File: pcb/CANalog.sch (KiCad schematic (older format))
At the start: 81 parts, among them J1 PWR, J4 STM_PROG, J5 ESP_PROG, J6 AOUT, J7 CAN, Q1 DMP3099L-7, SW1 RESET, SW2 ESP_PROG, U1 BL9342, U2 MIC5504-3.3YM5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

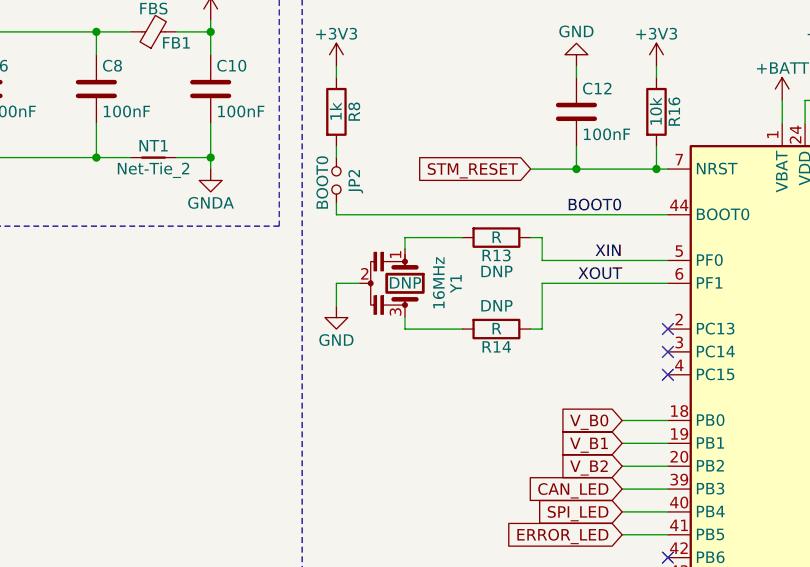
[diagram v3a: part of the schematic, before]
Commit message: update iBom with DNP fields missing
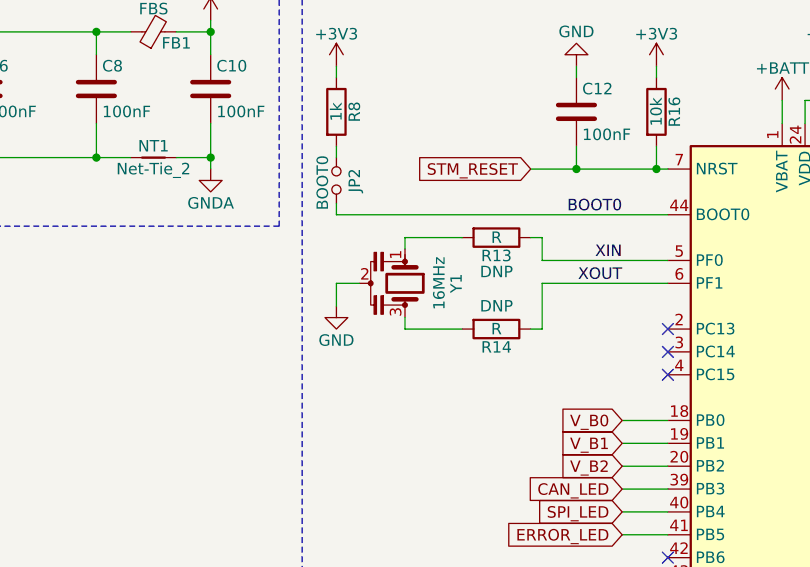
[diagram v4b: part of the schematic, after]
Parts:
- Y1: Population DNP -> (none)
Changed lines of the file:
@@
 F 2 "Crystal:Resonator_SMD_muRata_CSTxExxV-3Pin_3.0x1.1mm" H 6625 6200 50  0001 C CNN
 F 3 "https://www.mouser.com/datasheet/2/281/murata_04192018_CSTN_CeramResonCERAL-1323383.pdf" H 6625 6200 50  0001 C CNN
-F 4 "DNP" V 6650 6200 50  0000 C CNN "Population"
-F 5 "CSTNE16M0VH3C000R0 " H 6650 6200 50  0001 C CNN "MPN"
-F 6 "Murata Electronics" H 6650 6200 50  0001 C CNN "Manufacture"
-F 7 "81-CSTNE16M0VH3C000R " H 6650 6200 50  0001 C CNN "SPN"
-F 8 "Mouser" H 6650 6200 50  0001 C CNN "Supplier"
-F 9 "https://www.mouser.com/ProductDetail/81-CSTNE16M0VH3C000R" H 6650 6200 50  0001 C CNN "Supplier Link"
+F 4 "CSTNE16M0VH3C000R0 " H 6650 6200 50  0001 C CNN "MPN"
+F 5 "Murata Electronics" H 6650 6200 50  0001 C CNN "Manufacture"
+F 6 "81-CSTNE16M0VH3C000R " H 6650 6200 50  0001 C CNN "SPN"
+F 7 "Mouser" H 6650 6200 50  0001 C CNN "Supplier"
+F 8 "https://www.mouser.com/ProductDetail/81-CSTNE16M0VH3C000R" H 6650 6200 50  0001 C CNN "Supplier Link"
 	1    6650 6200
 	0    1    1    0

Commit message: fix ibom missing R21
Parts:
- R21: Population DNP -> (none)
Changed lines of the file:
@@
 F 2 "Resistor_SMD:R_0603_1608Metric" V 11580 2000 50  0001 C CNN
 F 3 "~" H 11650 2000 50  0001 C CNN
-F 4 "DNP" H 11650 2000 50  0001 C CNN "Population"
 	1    11650 2000
 	0    1    1    0

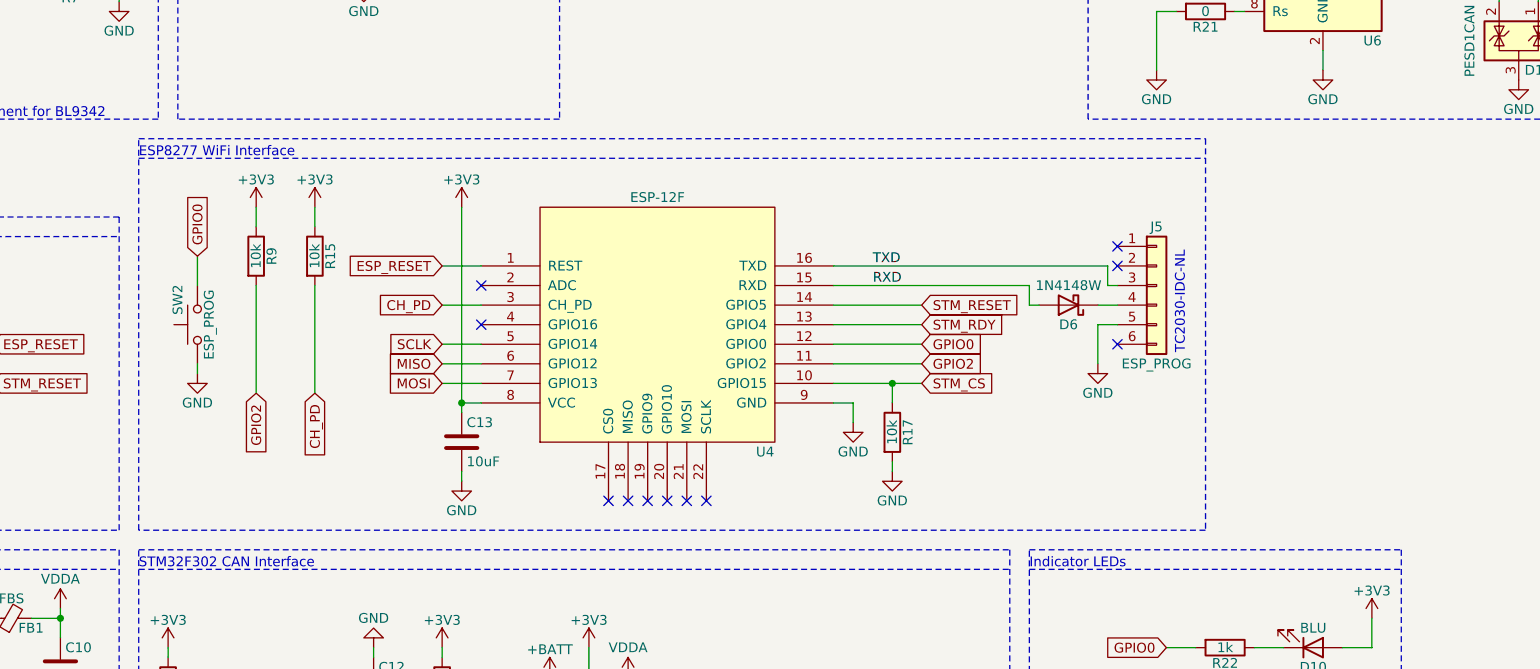
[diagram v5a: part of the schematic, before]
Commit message: added resistor between STM32 reset land ESP8266 GPIO15
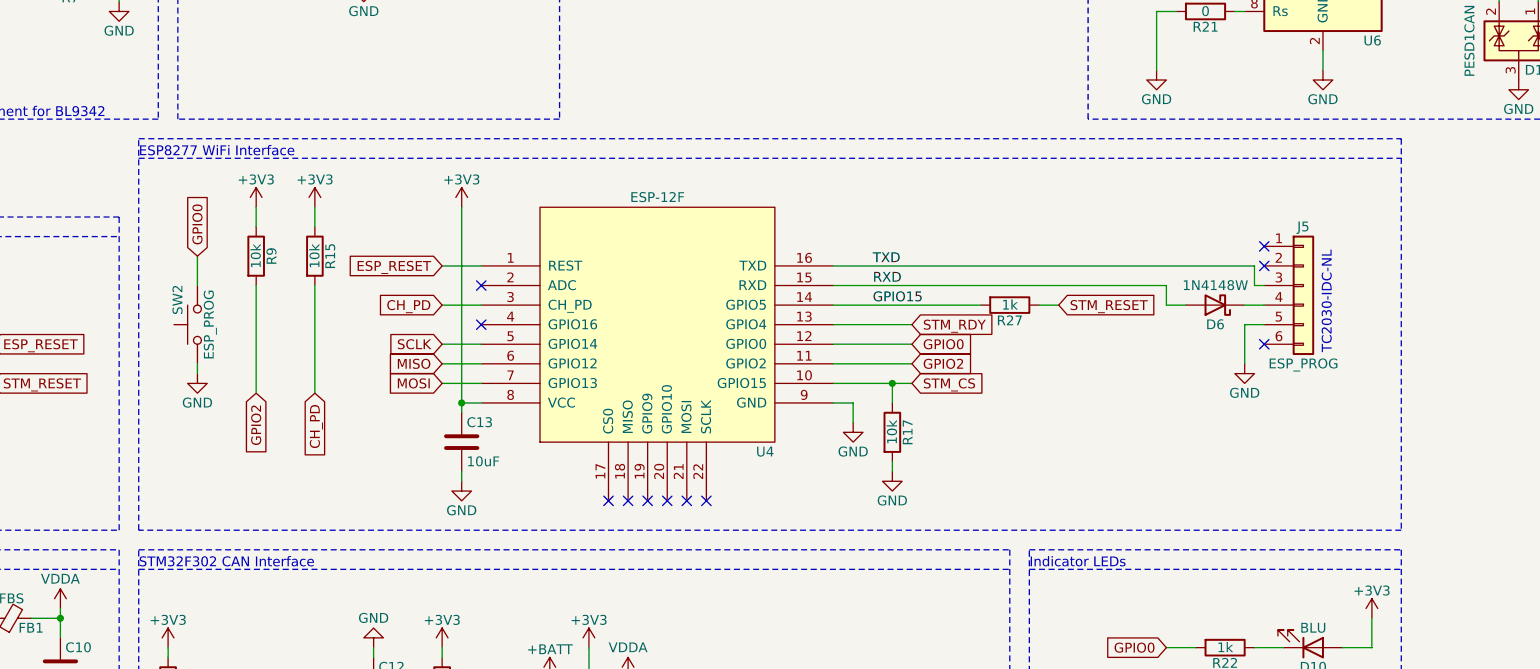
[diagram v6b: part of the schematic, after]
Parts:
- added R27: 1k, Resistor_SMD:R_0603_1608Metric, symbol Device:R
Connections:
- net STM_RESET: now also R27.1; no longer U4.14 (GPIO5)
- new net GPIO15: R27.2, U4.14 (GPIO5)
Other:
- moved on the sheet: D6, J5
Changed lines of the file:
@@
 $EndComp
 Wire Notes Line
-	11650 2650 11650 4650
+	12650 2650 12650 4650
 Text Label 9950 3400 0    50   ~ 0
 RXD
 Wire Wire Line
-	10750 3500 10750 3400
+	11450 3500 11450 3400
 Text Label 9950 3300 0    50   ~ 0
 TXD
 Wire Wire Line
-	9750 3300 11150 3300
+	9750 3300 11900 3300
 Wire Wire Line
 	10050 4350 10050 4300
@@
 Wire Wire Line
 	6800 3400 6800 3950
-Text GLabel 10200 3800 2    50   Input ~ 0
+Text GLabel 10150 3800 2    50   Input ~ 0
 GPIO2
 Wire Wire Line
-	10200 3800 9750 3800
+	10150 3800 9750 3800
 Text GLabel 6800 3950 3    50   Input ~ 0
 GPIO2
@@
 NoConn ~ 9000 4500
 NoConn ~ 9100 4500
-Text GLabel 10200 3900 2    50   Input ~ 0
+Text GLabel 10150 3900 2    50   Input ~ 0
 STM_CS
 Wire Wire Line
-	10200 3900 10050 3900
+	10150 3900 10050 3900
 $Comp
 L Switch:SW_Push SW2
@@
 ESP_RESET
 Wire Wire Line
-	9750 3700 10200 3700
-Text GLabel 10200 3700 2    50   Input ~ 0
+	9750 3700 10150 3700
+Text GLabel 10150 3700 2    50   Input ~ 0
 GPIO0
 $Comp
@@
 MOSI
 NoConn ~ 7950 3600
-Wire Wire Line
-	9750 3400 10750 3400
-Text GLabel 10200 3600 2    50   Input ~ 0
+Text GLabel 10150 3600 2    50   Input ~ 0
 STM_RDY
 Wire Wire Line
-	10200 3600 9750 3600
-Wire Wire Line
-	9750 3500 10200 3500
-Wire Notes Line
-	6200 2750 11650 2750
-Wire Notes Line
-	11650 4650 6200 4650
+	10150 3600 9750 3600
+Wire Notes Line
+	6200 2750 12650 2750
+Wire Notes Line
+	12650 4650 6200 4650
 Wire Notes Line
 	6200 4650 6200 2650
 Wire Notes Line
-	6200 2650 11650 2650
+	6200 2650 12650 2650
 $Comp
 L Connector_Generic:Conn_01x06 J5
 U 1 1 60FEC2BA
-P 11400 3400
-F 0 "J5" H 11400 3700 50  0000 C CNN
-F 1 "ESP_PROG" H 11400 3000 50  0000 C CNN
-F 2 "Connector:Tag-Connect_TC2030-IDC-NL_2x03_P1.27mm_Vertical" H 11400 3400 50  0001 C CNN
-F 3 "~" H 11400 3400 50  0001 C CNN
-F 4 "DNP" H 11400 3400 50  0001 C CNN "Population"
-	1    11400 3400
+P 12150 3400
+F 0 "J5" H 12150 3700 50  0000 C CNN
+F 1 "ESP_PROG" H 12150 3000 50  0000 C CNN
+F 2 "Connector:Tag-Connect_TC2030-IDC-NL_2x03_P1.27mm_Vertical" H 12150 3400 50  0001 C CNN
+F 3 "~" H 12150 3400 50  0001 C CNN
+F 4 "DNP" H 12150 3400 50  0001 C CNN "Population"
+	1    12150 3400
 	1    0    0    -1
 $EndComp
@@
 L power:GND #PWR049
 U 1 1 61023622
-P 11100 3800
-F 0 "#PWR049" H 11100 3550 50  0001 C CNN
-F 1 "GND" H 11100 3650 50  0000 C CNN
-F 2 "" H 11100 3800 50  0001 C CNN
-F 3 "" H 11100 3800 50  0001 C CNN
-	1    11100 3800
-	1    0    0    -1
-$EndComp
-NoConn ~ 11200 3200
-NoConn ~ 11200 3700
-NoConn ~ 11200 3300
-Wire Wire Line
-	10750 3500 10800 3500
-Wire Wire Line
-	11150 3400 11150 3300
+P 11850 3800
+F 0 "#PWR049" H 11850 3550 50  0001 C CNN
+F 1 "GND" H 11850 3650 50  0000 C CNN
+F 2 "" H 11850 3800 50  0001 C CNN
+F 3 "" H 11850 3800 50  0001 C CNN
+	1    11850 3800
+	1    0    0    -1
+$EndComp
+NoConn ~ 11950 3200
+NoConn ~ 11950 3700
+NoConn ~ 11950 3300
+Wire Wire Line
+	11450 3500 11550 3500
+Wire Wire Line
+	11900 3400 11900 3300
 Wire Notes Line
 	12650 6700 12650 9100
@@
 Text GLabel 5450 3900 2    50   Input ~ 0
 STM_RESET
-Text GLabel 10200 3500 2    50   Input ~ 0
+Text GLabel 10900 3500 2    50   Input ~ 0
 STM_RESET
 Wire Wire Line
@@
 L Device:D_Schottky D6
 U 1 1 606DDDEA
-P 10950 3500
-F 0 "D6" H 10950 3600 50  0000 C CNN
-F 1 "1N4148W" H 10950 3400 50  0000 C CNN
-F 2 "Diode_SMD:D_SOD-123" H 10950 3500 50  0001 C CNN
-F 3 "https://datasheet.lcsc.com/szlcsc/1809052017_MDD-Microdiode-Electronics-1N4148W_C84367.pdf" H 10950 3500 50  0001 C CNN
-F 4 "1N4148W" H 10950 3500 50  0001 C CNN "MPN"
-F 5 "Microdiode Electronics" H 10950 3500 50  0001 C CNN "Manufacture"
-F 6 "C84367" H 10950 3500 50  0001 C CNN "SPN"
-F 7 "LCSC" H 10950 3500 50  0001 C CNN "Supplier"
-F 8 "https://lcsc.com/product-detail/Switching-Diode_MDD-Microdiode-Electronics-1N4148W_C84367.html" H 10950 3500 50  0001 C CNN "Supplier Link"
-	1    10950 3500
+P 11700 3500
+F 0 "D6" H 11700 3600 50  0000 C CNN
+F 1 "1N4148W" H 11700 3400 50  0000 C CNN
+F 2 "Diode_SMD:D_SOD-123" H 11700 3500 50  0001 C CNN
+F 3 "https://datasheet.lcsc.com/szlcsc/1809052017_MDD-Microdiode-Electronics-1N4148W_C84367.pdf" H 11700 3500 50  0001 C CNN
+F 4 "1N4148W" H 11700 3500 50  0001 C CNN "MPN"
+F 5 "Microdiode Electronics" H 11700 3500 50  0001 C CNN "Manufacture"
+F 6 "C84367" H 11700 3500 50  0001 C CNN "SPN"
+F 7 "LCSC" H 11700 3500 50  0001 C CNN "Supplier"
+F 8 "https://lcsc.com/product-detail/Switching-Diode_MDD-Microdiode-Electronics-1N4148W_C84367.html" H 11700 3500 50  0001 C CNN "Supplier Link"
+	1    11700 3500
 	-1   0    0    1
 $EndComp
@@
 NoConn ~ 9100 7700
 Wire Wire Line
-	11100 3800 11100 3600
-Wire Wire Line
-	11100 3600 11200 3600
-Wire Wire Line
-	11200 3400 11150 3400
-Wire Wire Line
-	11100 3500 11200 3500
-Text Notes 11550 3750 1    50   ~ 0
+	11850 3800 11850 3600
+Wire Wire Line
+	11850 3600 11950 3600
+Wire Wire Line
+	11950 3400 11900 3400
+Wire Wire Line
+	11850 3500 11950 3500
+Text Notes 12300 3750 1    50   ~ 0
 TC2030-IDC-NL
 Text Notes 10550 8450 1    50   ~ 0
@@
 Wire Wire Line
 	9300 8300 9300 8500
+Wire Wire Line
+	9750 3500 10500 3500
+Wire Wire Line
+	10800 3500 10900 3500
+Wire Wire Line
+	9750 3400 11450 3400
+Text Label 9950 3500 0    50   ~ 0
+GPIO15
+$Comp
+L Device:R R27
+U 1 1 611F4478
+P 10650 3500
+F 0 "R27" V 10730 3500 50  0000 C CNN
+F 1 "1k" V 10650 3500 50  0000 C CNN
+F 2 "Resistor_SMD:R_0603_1608Metric" V 10580 3500 50  0001 C CNN
+F 3 "https://www.yageo.com/upload/media/product/productsearch/datasheet/rchip/PYu-RC_Group_51_RoHS_L_11.pdf" H 10650 3500 50  0001 C CNN
+F 4 "RC0603JR-071KL" H 10650 3500 50  0001 C CNN "MPN"
+F 5 "YAGEO" H 10650 3500 50  0001 C CNN "Manufacture"
+F 6 "311-1.0KGRCT-ND" H 10650 3500 50  0001 C CNN "SPN"
+F 7 "DigiKey" H 10650 3500 50  0001 C CNN "Supplier"
+F 8 "https://www.digikey.com/en/products/detail/yageo/RC0603JR-071KL/726677?s=N4IgTCBcDaIMwEYEFoEDoAMBrA5gJwGMAXZAOwBMQBdAXyA" H 10650 3500 50  0001 C CNN "Supplier Link"
+	1    10650 3500
+	0    1    1    0
+$EndComp
 $EndSCHEMATC

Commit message: add 16bit DAC
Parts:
- removed U5: OPA330xxDBV, Package_TO_SOT_SMD:SOT-23-5, symbol Amplifier_Operational:OPA330xxDBV
- added C19: 100nF, C_0603_1608Metric, symbol Device:C
- added R28: 1k, Resistor_SMD:R_0603_1608Metric, symbol Device:R
- added U5: DAC80501ZDGSR, Package_SO:VSSOP-10_3x3mm_P0.5mm, symbol pl_DAC:DAC80501ZDGSR
- R11: Population DNP -> (none)
- R12: Population (none) -> DNP
- R18: value 120k -> 10k; MPN RT0603BRD07120KL -> RC0603JR-0710KL; Population (none) -> DNP; SPN C705720 -> C99198; Supplier Link https://lcsc.com/product-detail/Chip-Resistor-Surface-Mount_YAGEO-RT0603BRD07120KL_C705720.html -> https://lcsc.com/product-detail/Chip-Resistor-Surface-Mount_YAGEO-RC0603JR-0710KL_C99198.html
- R19: value 12k -> 10k; MPN RT0603BRD0712KL -> RC0603JR-0710KL; Population (none) -> DNP; SPN C326735 -> C99198; Supplier Link https://lcsc.com/product-detail/Chip-Resistor-Surface-Mount_YAGEO-RT0603BRD0712KL_C326735.html -> https://lcsc.com/product-detail/Chip-Resistor-Surface-Mount_YAGEO-RC0603JR-0710KL_C99198.html
- R20: value 68k -> 1k; MPN RT0603BRD0768KL -> RC0603JR-071KL; SPN C705793 -> 311-1.0KGRCT-ND; Supplier LCSC -> DigiKey; Supplier Link https://lcsc.com/product-detail/Chip-Resistor-Surface-Mount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 -> https://www.digikey.com/en/products/detail/yageo/RC0603JR-0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
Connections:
- net +5V: now also R18.1, R19.1, R20.2, U5.1 (Vdd)
- net GNDA: now also C19.2, R28.2, U5.4 (AGND); no longer R19.2
- net at J6.1 (Pin_1): now also U5.2 (Vout); no longer R20.1
- net I2C_SCL: now reaches U3.16 (PA6)
- net I2C_SCL: now also R18.2, U5.6 (SCLK/SCL)
- net I2C_SDA: now reaches U3.17 (PA7)
- net I2C_SDA: now also R19.2, U5.8 (SDIN/SDA)
- net DAC: no longer names the net of U3.14 (PA4)
- new net: C19.1, U5.10 (VREFIO)
- new net: R20.1, U5.5 (SPI2C)
- new net: R28.1, U5.7 (~SYNC~/A0)
- no-connect marks 31 -> 30
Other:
- note added: "DAC 16bit - I2C Interface"
- note added: "DAC Bypass Capacitors"
- note added: "I2C 16bit DAC"
- note removed: "Analog Output Amplification"
- note removed: "G = 5.0/3.3\nG = 1 + (68k/[120k + 12k])"
- note removed: "OPA330 Bypass Capacitors"
- moved on the sheet: C16, C17, J6

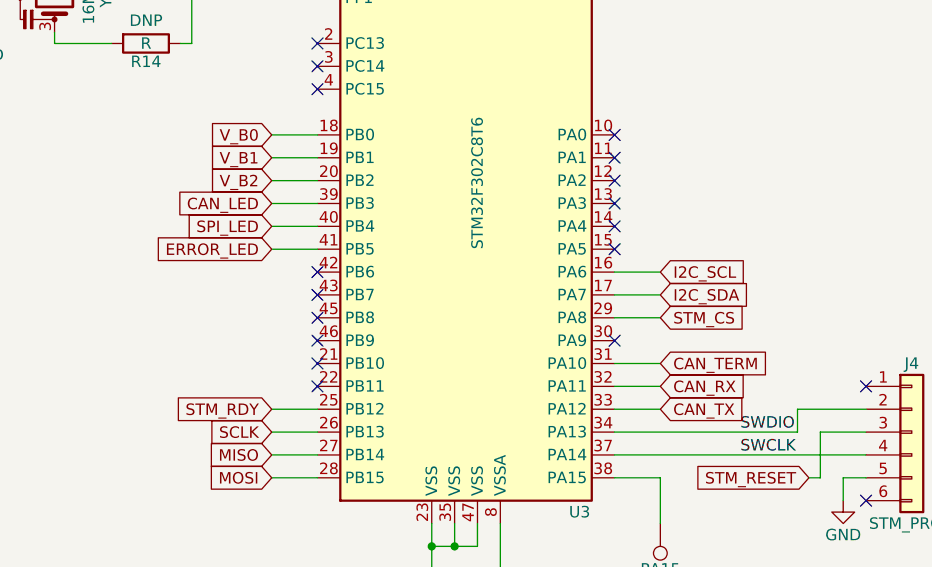
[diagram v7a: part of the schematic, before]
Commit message: add DAC
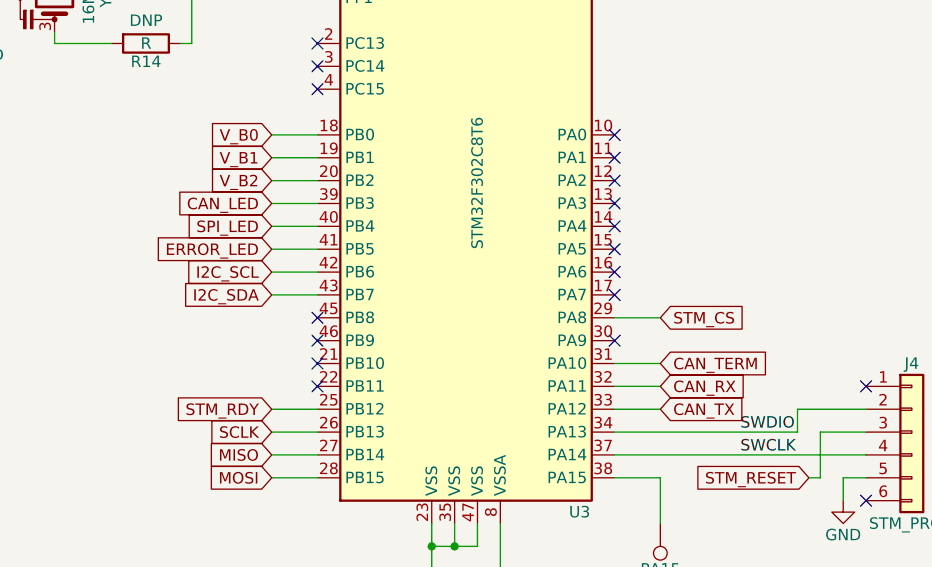
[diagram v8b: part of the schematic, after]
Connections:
- net I2C_SCL: now also U3.42 (PB6); no longer U3.16 (PA6)
- net I2C_SDA: now also U3.43 (PB7); no longer U3.17 (PA7)
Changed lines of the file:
@@
 Wire Wire Line
 	11400 2000 11500 2000
-NoConn ~ 7800 7400
 Wire Wire Line
 	10200 8100 10000 8100
@@
 Wire Wire Line
 	9100 7800 9300 7800
-NoConn ~ 7800 7500
 NoConn ~ 7800 7900
 Wire Wire Line
@@
 	1    0    0    -1
 $EndComp
-Text GLabel 9300 7400 2    50   Input ~ 0
+Text GLabel 7600 7400 0    50   Input ~ 0
 I2C_SCL
-Text GLabel 9300 7500 2    50   Input ~ 0
+Text GLabel 7600 7500 0    50   Input ~ 0
 I2C_SDA
-Wire Wire Line
-	9100 7400 9300 7400
-Wire Wire Line
-	9100 7500 9300 7500
 Text GLabel 11150 7550 0    50   Input ~ 0
 I2C_SCL
@@
 Wire Wire Line
 	750  10200 750  10050
+Wire Wire Line
+	7600 7400 7800 7400
+Wire Wire Line
+	7600 7500 7800 7500
+NoConn ~ 9100 7400
+NoConn ~ 9100 7500
 $EndSCHEMATC
